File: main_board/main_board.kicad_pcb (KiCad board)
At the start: 2 copper layers, 100 x 68.1 mm, 116 parts, among them J1 Conn_01x08_S8B-PH-K-S(LF)(SN), J2 Conn_02x20_2214SM-40G-75-PCR, J3 Conn_01x02_B2B-PH-K-S(LF)(SN), J4 USB_C_USB4930-00-A, J5 Conn_01x03_MC34747, J6 Conn_01x04_FFC3B11-04-T, Q1 Q_BC817-25, Q2 Q_FDC6561AN, Q3 Q_BC817-25, SW1 SW_B3FS-1050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

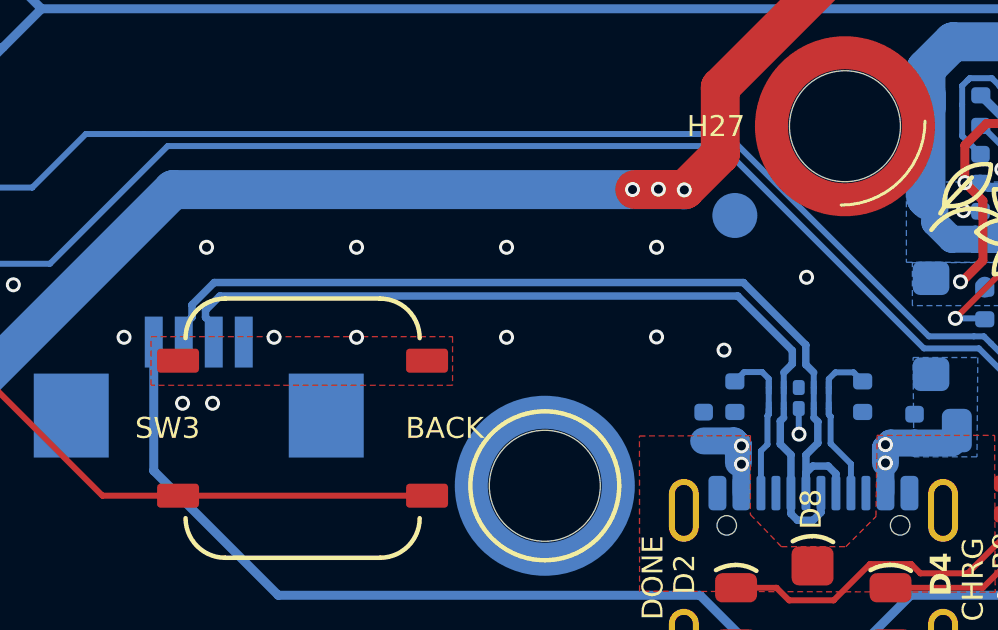
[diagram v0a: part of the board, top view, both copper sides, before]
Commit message: Fix differential pair clearence in board settings and GND pour
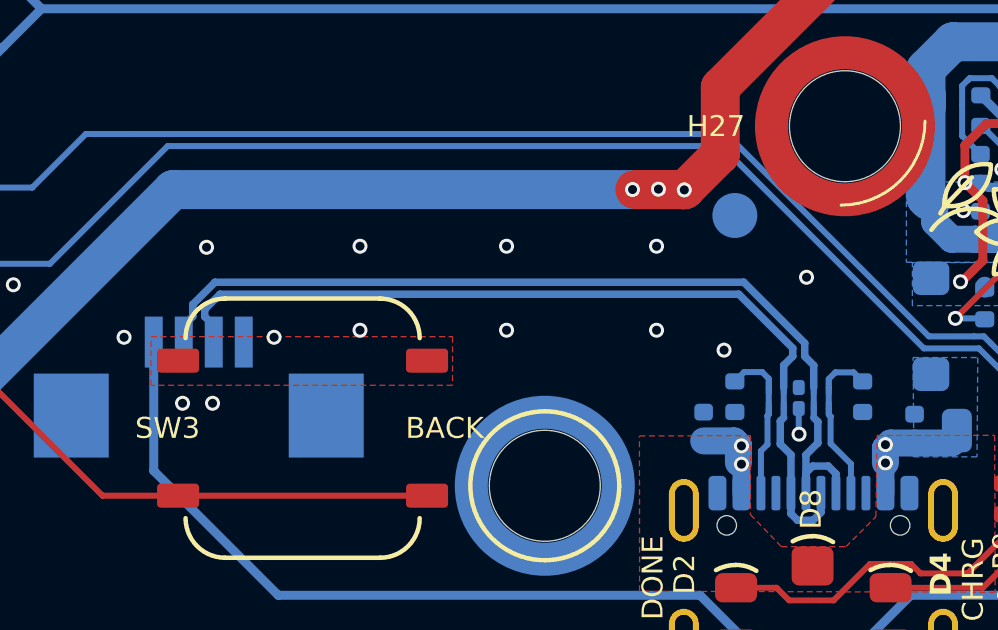
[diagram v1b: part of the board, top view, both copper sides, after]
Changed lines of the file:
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@@
 	)
 	(via
-		(at 165.485 121.804)
+		(at 165.485 121.769)
 		(size 0.5)
 		(drill 0.3)
@@
 	)
 	(via
-		(at 155.485 121.804)
+		(at 155.6 121.769)
 		(size 0.5)
 		(drill 0.3)
@@
 	)
 	(via
-		(at 155.485 124.804)
+		(at 155.6 124.569)
 		(size 0.5)
 		(drill 0.3)
@@
 	)
 	(via
-		(at 160.485 121.804)
+		(at 160.485 121.769)
 		(size 0.5)
 		(drill 0.3)
@@
 	)
 	(via
-		(at 165.485 124.794)
+		(at 165.485 124.569)
 		(size 0.5)
 		(drill 0.3)
@@
 	)
 	(via
-		(at 160.485 124.804)
+		(at 160.485 124.569)
 		(size 0.5)
 		(drill 0.3)
@@
 	)
 	(segment
-		(start 150.741802 122.979)
-		(end 150 123.720802)
-		(width 0.25)
-		(layer "B.Cu")
-		(net 41)
-	)
-	(segment
-		(start 170.46 125.060802)
-		(end 168.378198 122.979)
-		(width 0.25)
-		(layer "B.Cu")
-		(net 41)
-	)
-	(segment
 		(start 170.465 129.999)
 		(end 170.465 128.724)
@@
 	)
 	(segment
+		(start 170.725 125.739)
+		(end 170.425 125.439)
+		(width 0.25)
+		(layer "B.Cu")
+		(net 41)
+	)
+	(segment
 		(start 170.465 128.724)
 		(end 170.861 128.328)
@@
 	)
 	(segment
-		(start 171.465 129.354822)
-		(end 171.208178 129.098)
+		(start 168.392844 122.969)
+		(end 150.767156 122.969)
 		(width 0.25)
 		(layer "B.Cu")
@@
 	)
 	(segment
-		(start 170.725 125.979)
-		(end 170.725 126.479)
-		(width 0.2)
+		(start 171.465 129.354822)
+		(end 171.208178 129.098)
+		(width 0.25)
 		(layer "B.Cu")
 		(net 41)
 	)
 	(segment
-		(start 170.465 129.324)
-		(end 170.465 129.999)
+		(start 149.725 124.414)
+		(end 149.725 124.964)
 		(width 0.25)
 		(layer "B.Cu")
@@
 	)
 	(segment
-		(start 150 124.139)
-		(end 149.725 124.414)
+		(start 170.465 129.324)
+		(end 170.465 129.999)
 		(width 0.25)
 		(layer "B.Cu")
@@
 	)
 	(segment
-		(start 170.46 125.714)
-		(end 170.46 125.060802)
+		(start 150.025 124.114)
+		(end 149.725 124.414)
 		(width 0.25)
 		(layer "B.Cu")
@@
 	)
 	(segment
-		(start 149.725 124.414)
-		(end 149.725 124.964)
+		(start 170.425 125.439)
+		(end 170.425 125.001156)
 		(width 0.25)
 		(layer "B.Cu")
@@
 	)
 	(segment
-		(start 168.378198 122.979)
-		(end 150.741802 122.979)
+		(start 170.425 125.001156)
+		(end 168.392844 122.969)
 		(width 0.25)
 		(layer "B.Cu")
@@
 	)
 	(segment
-		(start 150 123.720802)
-		(end 150 124.139)
+		(start 170.725 126.479)
+		(end 170.725 125.739)
 		(width 0.25)
 		(layer "B.Cu")
@@
 	)
 	(segment
+		(start 150.767156 122.969)
+		(end 150.025 123.711156)
+		(width 0.25)
+		(layer "B.Cu")
+		(net 41)
+	)
+	(segment
 		(start 170.725 127.179)
 		(end 170.725 127.482226)
@@
 	)
 	(segment
-		(start 170.725 125.979)
-		(end 170.46 125.714)
+		(start 150.025 123.711156)
+		(end 150.025 124.114)
 		(width 0.25)
 		(layer "B.Cu")
@@
 	)
 	(segment
-		(start 170.704178 130.904)
-		(end 170.965 130.643178)
+		(start 150.425 124.114)
+		(end 150.725 124.414)
 		(width 0.25)
 		(layer "B.Cu")
@@
 	)
 	(segment
-		(start 170.01 125.694)
-		(end 169.725 125.979)
+		(start 170.704178 130.904)
+		(end 170.965 130.643178)
 		(width 0.25)
 		(layer "B.Cu")
@@
 	)
 	(segment
-		(start 150.928198 123.429)
-		(end 168.191802 123.429)
-		(width 0.25)
-		(layer "B.Cu")
-		(net 42)
-	)
-	(segment
 		(start 169.965 130.684)
 		(end 170.185 130.904)
@@
 	)
 	(segment
-		(start 168.191802 123.429)
-		(end 170.01 125.247198)
+		(start 170.025 125.439)
+		(end 170.025 125.166844)
 		(width 0.25)
 		(layer "B.Cu")
@@
 	)
 	(segment
-		(start 170.01 125.247198)
-		(end 170.01 125.694)
+		(start 150.425 123.876844)
+		(end 150.425 124.114)
 		(width 0.25)
 		(layer "B.Cu")
@@
 	)
 	(segment
-		(start 169.725 126.479)
-		(end 169.725 125.979)
-		(width 0.2)
+		(start 169.965 129.999)
+		(end 169.965 130.684)
+		(width 0.25)
 		(layer "B.Cu")
 		(net 42)
 	)
 	(segment
-		(start 169.965 129.999)
-		(end 169.965 130.684)
+		(start 170.025 125.166844)
+		(end 168.227156 123.369)
 		(width 0.25)
 		(layer "B.Cu")
@@
 	)
 	(segment
-		(start 150.45 124.139)
-		(end 150.45 123.907198)
+		(start 169.965 128.719)
+		(end 169.609 128.363)
 		(width 0.25)
 		(layer "B.Cu")
@@
 	)
 	(segment
-		(start 169.965 128.719)
-		(end 169.609 128.363)
+		(start 169.609 128.363)
+		(end 169.609 127.598226)
 		(width 0.25)
 		(layer "B.Cu")
@@
 	)
 	(segment
-		(start 169.609 128.363)
-		(end 169.609 127.598226)
+		(start 169.725 126.479)
+		(end 169.725 125.739)
 		(width 0.25)
 		(layer "B.Cu")
@@
 	)
 	(segment
-		(start 150.45 123.907198)
-		(end 150.928198 123.429)
+		(start 169.965 129.999)
+		(end 169.965 128.719)
 		(width 0.25)
 		(layer "B.Cu")
@@
 	)
 	(segment
-		(start 150.725 124.414)
-		(end 150.45 124.139)
+		(start 150.932844 123.369)
+		(end 150.425 123.876844)
 		(width 0.25)
 		(layer "B.Cu")
@@
 	)
 	(segment
-		(start 169.965 129.999)
-		(end 169.965 128.719)
+		(start 168.227156 123.369)
+		(end 150.932844 123.369)
 		(width 0.25)
 		(layer "B.Cu")
@@
 	)
 	(segment
-		(start 150.725 124.964)
-		(end 150.725 124.414)
+		(start 150.725 124.414)
+		(end 150.725 124.964)
+		(width 0.25)
+		(layer "B.Cu")
+		(net 42)
+	)
+	(segment
+		(start 169.725 125.739)
+		(end 170.025 125.439)
 		(width 0.25)
 		(layer "B.Cu")
@@
 		(priority 1)
 		(connect_pads
-			(clearance 0.2)
+			(clearance 0.15)
 		)
 		(min_thickness 0.2)
@@
 		(priority 1)
 		(connect_pads
-			(clearance 0.2)
+			(clearance 0.15)
 		)
 		(min_thickness 0.2)
